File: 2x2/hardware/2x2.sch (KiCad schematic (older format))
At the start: 20 parts

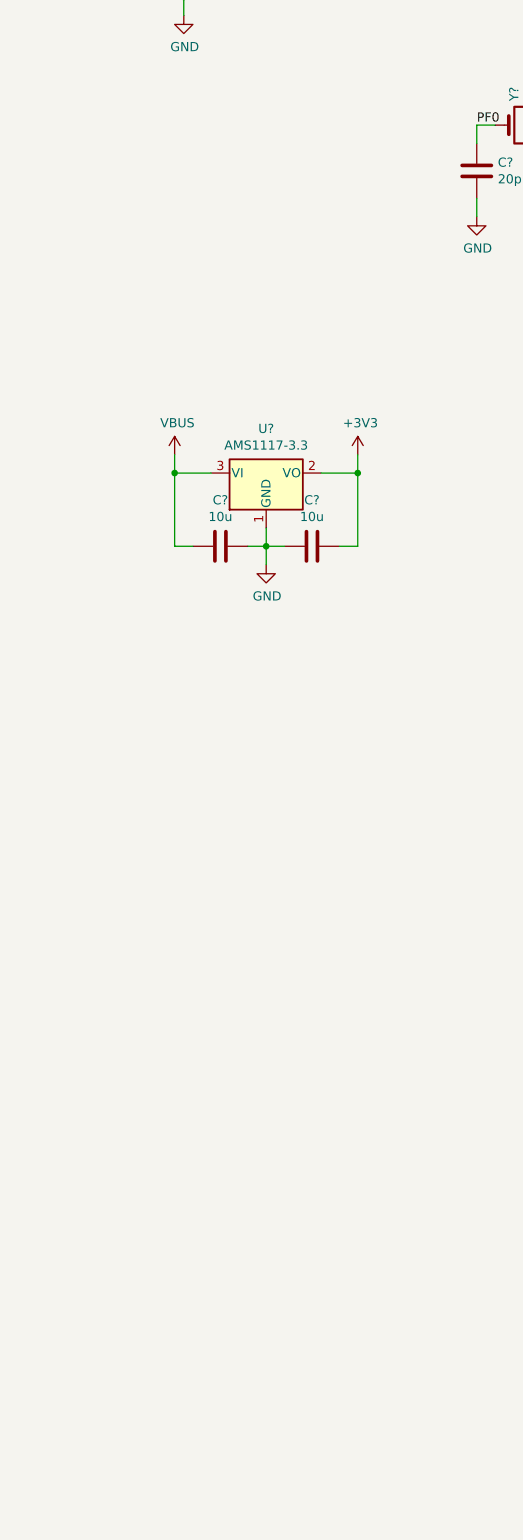
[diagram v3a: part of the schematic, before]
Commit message: Add 4 mounting holes
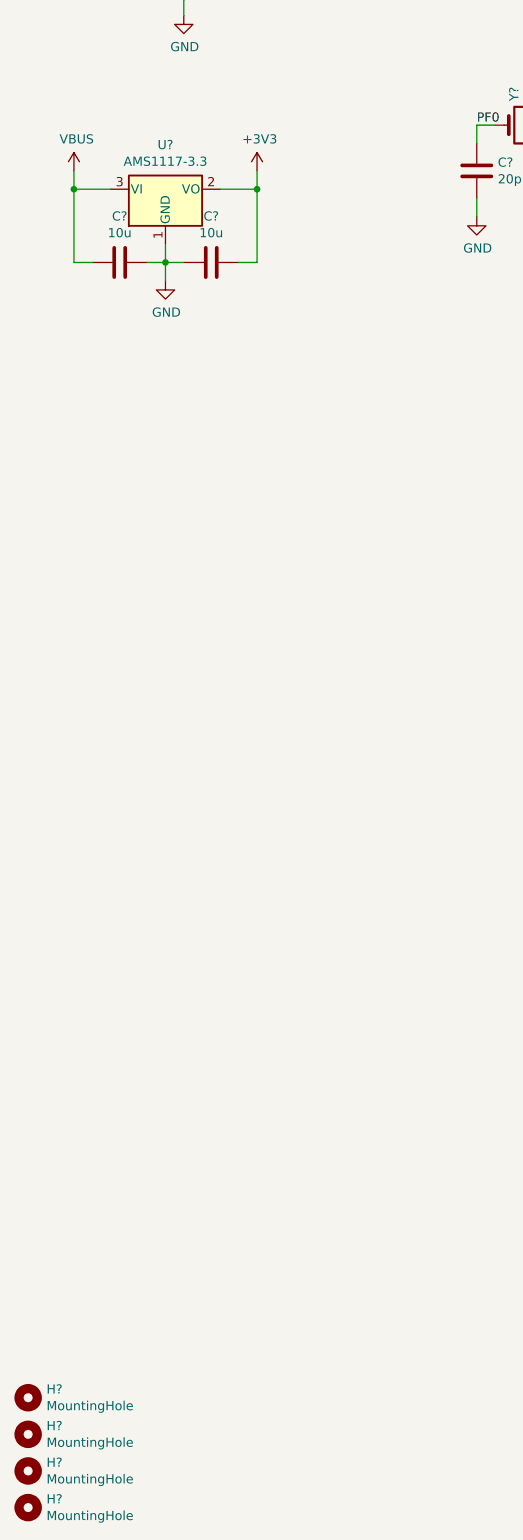
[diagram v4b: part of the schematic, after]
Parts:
- added H? (x4): MountingHole, symbol Mechanical:MountingHole
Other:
- moved on the sheet: C?, U?
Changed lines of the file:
@@
 L Regulator_Linear:AMS1117-3.3 U?
 U 1 1 5E25DF5D
-P 1950 5350
-F 0 "U?" H 1950 5592 50  0000 C CNN
-F 1 "AMS1117-3.3" H 1950 5501 50  0000 C CNN
-F 2 "Package_TO_SOT_SMD:SOT-223-3_TabPin2" H 1950 5550 50  0001 C CNN
-F 3 "http://www.advanced-monolithic.com/pdf/ds1117.pdf" H 2050 5100 50  0001 C CNN
-	1    1950 5350
+P 1400 3800
+F 0 "U?" H 1400 4042 50  0000 C CNN
+F 1 "AMS1117-3.3" H 1400 3951 50  0000 C CNN
+F 2 "Package_TO_SOT_SMD:SOT-223-3_TabPin2" H 1400 4000 50  0001 C CNN
+F 3 "http://www.advanced-monolithic.com/pdf/ds1117.pdf" H 1500 3550 50  0001 C CNN
+	1    1400 3800
 	1    0    0    -1
 $EndComp
@@
 L power:GND #PWR?
 U 1 1 5E271B38
-P 1950 5850
-F 0 "#PWR?" H 1950 5600 50  0001 C CNN
-F 1 "GND" H 1955 5677 50  0000 C CNN
-F 2 "" H 1950 5850 50  0001 C CNN
-F 3 "" H 1950 5850 50  0001 C CNN
-	1    1950 5850
+P 1400 4300
+F 0 "#PWR?" H 1400 4050 50  0001 C CNN
+F 1 "GND" H 1405 4127 50  0000 C CNN
+F 2 "" H 1400 4300 50  0001 C CNN
+F 3 "" H 1400 4300 50  0001 C CNN
+	1    1400 4300
 	1    0    0    -1
 $EndComp
@@
 L power:VBUS #PWR?
 U 1 1 5E272465
-P 1450 5250
-F 0 "#PWR?" H 1450 5100 50  0001 C CNN
-F 1 "VBUS" H 1465 5423 50  0000 C CNN
-F 2 "" H 1450 5250 50  0001 C CNN
-F 3 "" H 1450 5250 50  0001 C CNN
-	1    1450 5250
+P 900 3700
+F 0 "#PWR?" H 900 3550 50  0001 C CNN
+F 1 "VBUS" H 915 3873 50  0000 C CNN
+F 2 "" H 900 3700 50  0001 C CNN
+F 3 "" H 900 3700 50  0001 C CNN
+	1    900  3700
 	1    0    0    -1
 $EndComp
@@
 L power:+3V3 #PWR?
 U 1 1 5E2729E2
-P 2450 5250
-F 0 "#PWR?" H 2450 5100 50  0001 C CNN
-F 1 "+3V3" H 2465 5423 50  0000 C CNN
-F 2 "" H 2450 5250 50  0001 C CNN
-F 3 "" H 2450 5250 50  0001 C CNN
-	1    2450 5250
+P 1900 3700
+F 0 "#PWR?" H 1900 3550 50  0001 C CNN
+F 1 "+3V3" H 1915 3873 50  0000 C CNN
+F 2 "" H 1900 3700 50  0001 C CNN
+F 3 "" H 1900 3700 50  0001 C CNN
+	1    1900 3700
 	1    0    0    -1
 $EndComp
@@
 L Device:C C?
 U 1 1 5E279D7D
-P 1700 5750
-F 0 "C?" V 1448 5750 50  0000 C CNN
-F 1 "10u" V 1539 5750 50  0000 C CNN
-F 2 "" H 1738 5600 50  0001 C CNN
-F 3 "~" H 1700 5750 50  0001 C CNN
-	1    1700 5750
+P 1150 4200
+F 0 "C?" V 898 4200 50  0000 C CNN
+F 1 "10u" V 989 4200 50  0000 C CNN
+F 2 "" H 1188 4050 50  0001 C CNN
+F 3 "~" H 1150 4200 50  0001 C CNN
+	1    1150 4200
 	0    1    1    0
 $EndComp
@@
 L Device:C C?
 U 1 1 5E27AF32
-P 2200 5750
-F 0 "C?" V 1948 5750 50  0000 C CNN
-F 1 "10u" V 2039 5750 50  0000 C CNN
-F 2 "" H 2238 5600 50  0001 C CNN
-F 3 "~" H 2200 5750 50  0001 C CNN
-	1    2200 5750
+P 1650 4200
+F 0 "C?" V 1398 4200 50  0000 C CNN
+F 1 "10u" V 1489 4200 50  0000 C CNN
+F 2 "" H 1688 4050 50  0001 C CNN
+F 3 "~" H 1650 4200 50  0001 C CNN
+	1    1650 4200
 	0    1    1    0
 $EndComp
 Wire Wire Line
-	2450 5250 2450 5350
+	1900 3700 1900 3800
 Wire Wire Line
-	2450 5350 2250 5350
+	1900 3800 1700 3800
 Wire Wire Line
-	2350 5750 2450 5750
+	1800 4200 1900 4200
 Wire Wire Line
-	2450 5750 2450 5350
-Connection ~ 2450 5350
+	1900 4200 1900 3800
+Connection ~ 1900 3800
 Wire Wire Line
-	1950 5650 1950 5750
+	1400 4100 1400 4200
 Wire Wire Line
-	2050 5750 1950 5750
-Connection ~ 1950 5750
+	1500 4200 1400 4200
+Connection ~ 1400 4200
 Wire Wire Line
-	1950 5750 1950 5850
+	1400 4200 1400 4300
 Wire Wire Line
-	1850 5750 1950 5750
+	1300 4200 1400 4200
 Wire Wire Line
-	1550 5750 1450 5750
+	1000 4200 900  4200
 Wire Wire Line
-	1450 5750 1450 5350
+	900  4200 900  3800
 Wire Wire Line
-	1650 5350 1450 5350
-Connection ~ 1450 5350
+	1100 3800 900  3800
+Connection ~ 900  3800
 Wire Wire Line
-	1450 5350 1450 5250
+	900  3800 900  3700
+$Comp
+L Mechanical:MountingHole H?
+U 1 1 5E2A13A4
+P 650 10400
+F 0 "H?" H 750 10446 50  0000 L CNN
+F 1 "MountingHole" H 750 10355 50  0000 L CNN
+F 2 "" H 650 10400 50  0001 C CNN
+F 3 "~" H 650 10400 50  0001 C CNN
+	1    650  10400
+	1    0    0    -1
+$EndComp
+$Comp
+L Mechanical:MountingHole H?
+U 1 1 5E2A26D8
+P 650 10600
+F 0 "H?" H 750 10646 50  0000 L CNN
+F 1 "MountingHole" H 750 10555 50  0000 L CNN
+F 2 "" H 650 10600 50  0001 C CNN
+F 3 "~" H 650 10600 50  0001 C CNN
+	1    650  10600
+	1    0    0    -1
+$EndComp
+$Comp
+L Mechanical:MountingHole H?
+U 1 1 5E2A2954
+P 650 10800
+F 0 "H?" H 750 10846 50  0000 L CNN
+F 1 "MountingHole" H 750 10755 50  0000 L CNN
+F 2 "" H 650 10800 50  0001 C CNN
+F 3 "~" H 650 10800 50  0001 C CNN
+	1    650  10800
+	1    0    0    -1
+$EndComp
+$Comp
+L Mechanical:MountingHole H?
+U 1 1 5E2A2B41
+P 650 11000
+F 0 "H?" H 750 11046 50  0000 L CNN
+F 1 "MountingHole" H 750 10955 50  0000 L CNN
+F 2 "" H 650 11000 50  0001 C CNN
+F 3 "~" H 650 11000 50  0001 C CNN
+	1    650  11000
+	1    0    0    -1
+$EndComp
 $EndSCHEMATC
